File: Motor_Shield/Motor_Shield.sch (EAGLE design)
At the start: 28 parts, among them U1 MOCD213, U2 MOCD213, U3 MOCD213, U4 ARDUINO_SHIELDLABEL, X1 2510-, X2 2510-, X5 C-GRID-05-15-91, X6 C-GRID-05-15-91

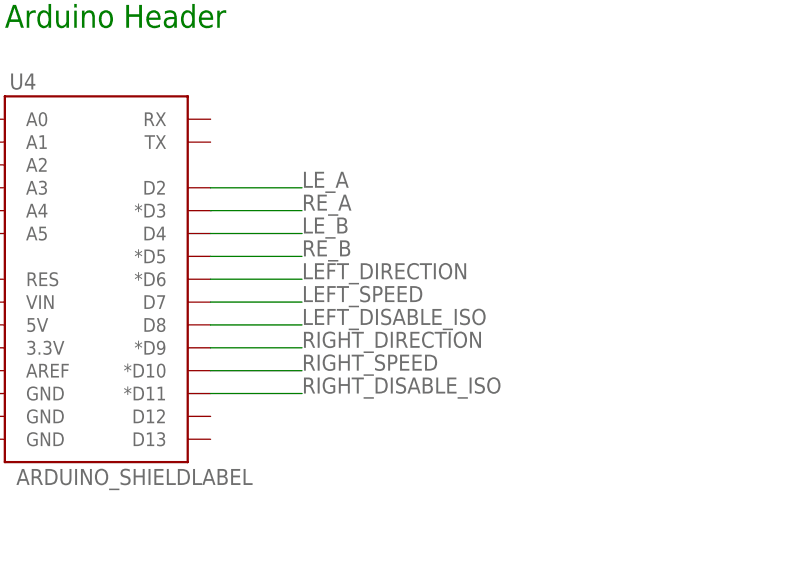
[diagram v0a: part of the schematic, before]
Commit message: Edited modified board design, pinout fixed
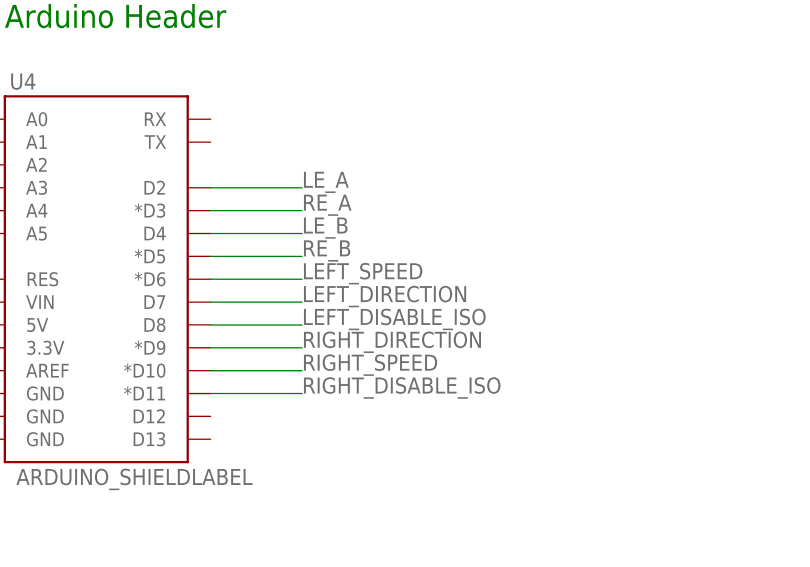
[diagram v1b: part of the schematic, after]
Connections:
- net LEFT_DIRECTION: now also U4.D7; no longer U4.*D6
- net LEFT_SPEED: now also U4.*D6; no longer U4.D7
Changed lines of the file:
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@@
 <?xml version="1.0" encoding="utf-8"?>
 <!DOCTYPE eagle SYSTEM "eagle.dtd">
-<eagle version="6.4">
+<eagle version="7.4.0">
 <drawing>
 <settings>
@@
 <net name="LEFT_SPEED" class="0">
 <segment>
-<pinref part="U4" gate="G$1" pin="D7"/>
-<wire x1="124.46" y1="187.96" x2="134.62" y2="187.96" width="0.1524" layer="91"/>
-<label x="134.62" y="187.96" size="1.778" layer="95"/>
-</segment>
-<segment>
 <pinref part="R1" gate="G$1" pin="1"/>
 <wire x1="274.32" y1="157.48" x2="266.7" y2="157.48" width="0.1524" layer="91"/>
 <label x="266.7" y="157.48" size="1.778" layer="95" rot="R180"/>
+</segment>
+<segment>
+<pinref part="U4" gate="G$1" pin="*D6"/>
+<wire x1="124.46" y1="190.5" x2="134.62" y2="190.5" width="0.1524" layer="91"/>
+<label x="134.62" y="190.5" size="1.778" layer="95"/>
 </segment>
 </net>
@@
 <net name="LEFT_DIRECTION" class="0">
 <segment>
-<pinref part="U4" gate="G$1" pin="*D6"/>
-<wire x1="124.46" y1="190.5" x2="134.62" y2="190.5" width="0.1524" layer="91"/>
-<label x="134.62" y="190.5" size="1.778" layer="95"/>
-</segment>
-<segment>
 <pinref part="R2" gate="G$1" pin="1"/>
 <wire x1="203.2" y1="157.48" x2="193.04" y2="157.48" width="0.1524" layer="91"/>
 <label x="195.58" y="157.48" size="1.778" layer="95" rot="R180"/>
 </segment>
-</net>
+<segment>
+<pinref part="U4" gate="G$1" pin="D7"/>
+<wire x1="124.46" y1="187.96" x2="134.62" y2="187.96" width="0.1524" layer="91"/>
+<label x="134.62" y="187.96" size="1.778" layer="95"/>
+</segment>
+</net>
